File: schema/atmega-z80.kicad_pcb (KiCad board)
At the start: 2 copper layers, 62 parts, among them J1 USB Connector, J2 ISP Connector, Q1 PNP_2N4403, Q2 PNP_2N4403, Q3 NPN_2N4401, Q4 PNP_2N4403, U1 Z84C0010PEG, U2 ATmega324A-PU, U3 AS6C4008-55PCN, U4 SN74HC373N, U5 SN74HC257, U6 SN74HC257, U7 SN74HC00, U8 MCP2221AxP, Y1 20MHz

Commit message: update LED resistors
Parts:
- J2: value ISP Connector -> SPI Connector
- R16, R17: value 120 -> 220
- R18, R20: value 100 -> 200
- R22: value 100 -> 220
- R23: value 68 -> 200
- R25: value 22 -> 1K

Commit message: Preliminary PCB layout
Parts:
- removed the C10 at (122.7, 128.8)
- removed the R13 at (113.8, 92.7)
- added C8: 0.1uF, Capacitor_SMD:C_1206_3216Metric_Pad1.33x1.80mm_HandSolder, F.Cu at (113.5, 145.8)
- added D8: 1N5817, Diode_THT:D_DO-41_SOD81_P10.16mm_Horizontal, F.Cu at (142.7, 139.2)
- added D9: 1N5817, Diode_THT:D_DO-41_SOD81_P10.16mm_Horizontal, F.Cu at (142.7, 135.9)
- added J3: SPI Connector, Connector_PinHeader_2.54mm:PinHeader_1x06_P2.54mm_Vertical, F.Cu at (122.6, 45.1)
- added J4: I2C Connector, Connector_PinHeader_2.54mm:PinHeader_1x04_P2.54mm_Vertical, F.Cu at (122.7, 85.1)
- added R11: 10K, Resistor_SMD:R_1206_3216Metric_Pad1.30x1.75mm_HandSolder, F.Cu at (134.5, 53.0)
- added R14: 10K, Resistor_SMD:R_1206_3216Metric_Pad1.30x1.75mm_HandSolder, F.Cu at (137.1, 85.1)
- added R17: 39, Resistor_SMD:R_1206_3216Metric_Pad1.30x1.75mm_HandSolder, F.Cu at (110.1, 92.7)
- D1, D2, D3, D4, D5, D6, D7: footprint LED_THT:LED_D3.0mm -> LED_THT:LED_D5.0mm
- J2: value SPI Connector -> Programmer ISP 10
- R15: value 39 -> 10K
- moved R6 54.3 mm to (165.1, 45.0), turned to 180 degrees
- moved R7 54.2 mm to (165.1, 41.4), turned to 180 degrees
- moved R15 42.9 mm to (137.1, 92.7), turned to 0 degrees
- moved R12 34.9 mm to (134.5, 56.6)
- moved U4 32.8 mm to (179.7, 124.2), turned to 180 degrees
- moved U6 32.4 mm to (153.0, 124.3), turned to 180 degrees
- moved C5 31.4 mm to (208.7, 108.2), turned to 270 degrees
- moved U3 27.7 mm to (189.6, 44.5)
- moved SW_RESET1 25.9 mm to (99.1, 148.6)
- moved SW_USER1 25.9 mm to (80.5, 144.0)
- moved R5 24.3 mm to (165.1, 48.5)
- moved R4 24.3 mm to (165.1, 52.1)
- moved R3 24.3 mm to (165.1, 55.6)
- moved R2 24.2 mm to (165.1, 58.9)
- moved R1 24.2 mm to (165.1, 62.2)
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- renumbered C11 to C10, C12 to C11, C13 to C12, R11 to R13, R14 to R16, R16 to R18, R17 to R19, R18 to R20, R19 to R21, R20 to R22, R21 to R23, R22 to R24, R23 to R25, R24 to R26, R25 to R27, R26 to R28
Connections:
- net /SPI_MISO renamed SPI_MISO
- net /SPI_MOSI renamed SPI_MOSI
- net /SPI_SCK renamed SPI_SCK
- C9 pad 1: Net-(C9-Pad1) -> +5V
- R1 pad 2: /A6 -> /A4
- R10 pad 2: /A15 -> /A13
- R12 pad 1: +5V -> GND
- R12 pad 2: /#NMI -> /A15
- R15 pad 1: /#Z80_CLK -> +5V
- R15 pad 2: Net-(R15-Pad2) -> /#IORQ
- R2 pad 2: /A7 -> /A5
- R3 pad 2: /A8 -> /A6
- R4 pad 2: /A9 -> /A7
- R5 pad 2: /A10 -> /A8
- R6 pad 2: /A11 -> /A9
- R7 pad 2: /A12 -> /A10
- R8 pad 2: /A13 -> /A11
- R9 pad 2: /A14 -> /A12
- U2 pad 1: /A3 -> /A0
- U2 pad 14: /UART_RXD -> /ATMEGA_RX_AND_USB_TX
- U2 pad 15: /UART_TXD -> /ATMEGA_TX_AND_USB_RX
- U2 pad 2: /A4 -> /A1
- U2 pad 21: Net-(R15-Pad2) -> Net-(R17-Pad2)
- U2 pad 22: /D0 -> I2C_SCL
- U2 pad 23: /D1 -> I2C_SDA
- U2 pad 24: /D2 -> /#INT
- U2 pad 25: /D3 -> /#BUSRQ
- U2 pad 26: /D4 -> /#BUSACK
- U2 pad 27: /D5 -> /#WAIT
- U2 pad 28: /D6 -> /#R
- U2 pad 29: /D7 -> /CHANGE_BANK_ADDR
- U2 pad 3: /A5 -> /A2
- U2 pad 33: /A2 -> /D7
- U2 pad 34: /A1 -> /D6
- U2 pad 35: /A0 -> /D5
- U2 pad 36: /#R -> /D4
- U2 pad 37: /#WAIT -> /D3
- U2 pad 38: /#BUSACK -> /D2
- U2 pad 39: /#BUSRQ -> /D1
- U2 pad 4: /CHANGE_BANK_ADDR -> /A3
- U2 pad 40: /#INT -> /D0
- U2 pad 5: Net-(U2-Pad5) -> #SPI_SS
- U8 pad 11: Net-(C9-Pad1) -> Net-(C8-Pad1)
- U8 pad 3: USB_IO_LED -> Net-(D8-Pad2)
- U8 pad 5: /UART_RXD -> /ATMEGA_TX_AND_USB_RX
- U8 pad 6: /UART_TXD -> /ATMEGA_RX_AND_USB_TX
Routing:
- net +5V: track 0.00 -> 611.4 mm, vias 0 -> 1
- net #MEM_LED: track 0.00 -> 146.2 mm, vias 0 -> 6
- net /#SYS_RESET: track 0.00 -> 143.2 mm, vias 0 -> 1
- net /A3: track 0.00 -> 143.1 mm
- net /A2: track 0.00 -> 140.2 mm
- net /A1: track 0.00 -> 137.7 mm
- net /A0: track 0.00 -> 135.2 mm
- net /D7: track 0.00 -> 123.6 mm, vias 0 -> 1
- net #EXT_MEM_LED: track 0.00 -> 120.8 mm, vias 0 -> 2
- net /D0: track 0.00 -> 118.6 mm, vias 0 -> 3
- net /D6: track 0.00 -> 116.0 mm
- net /D1: track 0.00 -> 111.7 mm, vias 0 -> 3
- net /D4: track 0.00 -> 106.7 mm
- net /D5: track 0.00 -> 105.5 mm
- net /D2: track 0.00 -> 96.6 mm, vias 0 -> 2
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- added copper zone on B.Cu, net GND
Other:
- board outline added: 142.2 x 115.6 mm
- net class Power added: clearance 0.2, trace_width 0.5, via_dia 0.8, via_drill 0.4
- board text added: "+"

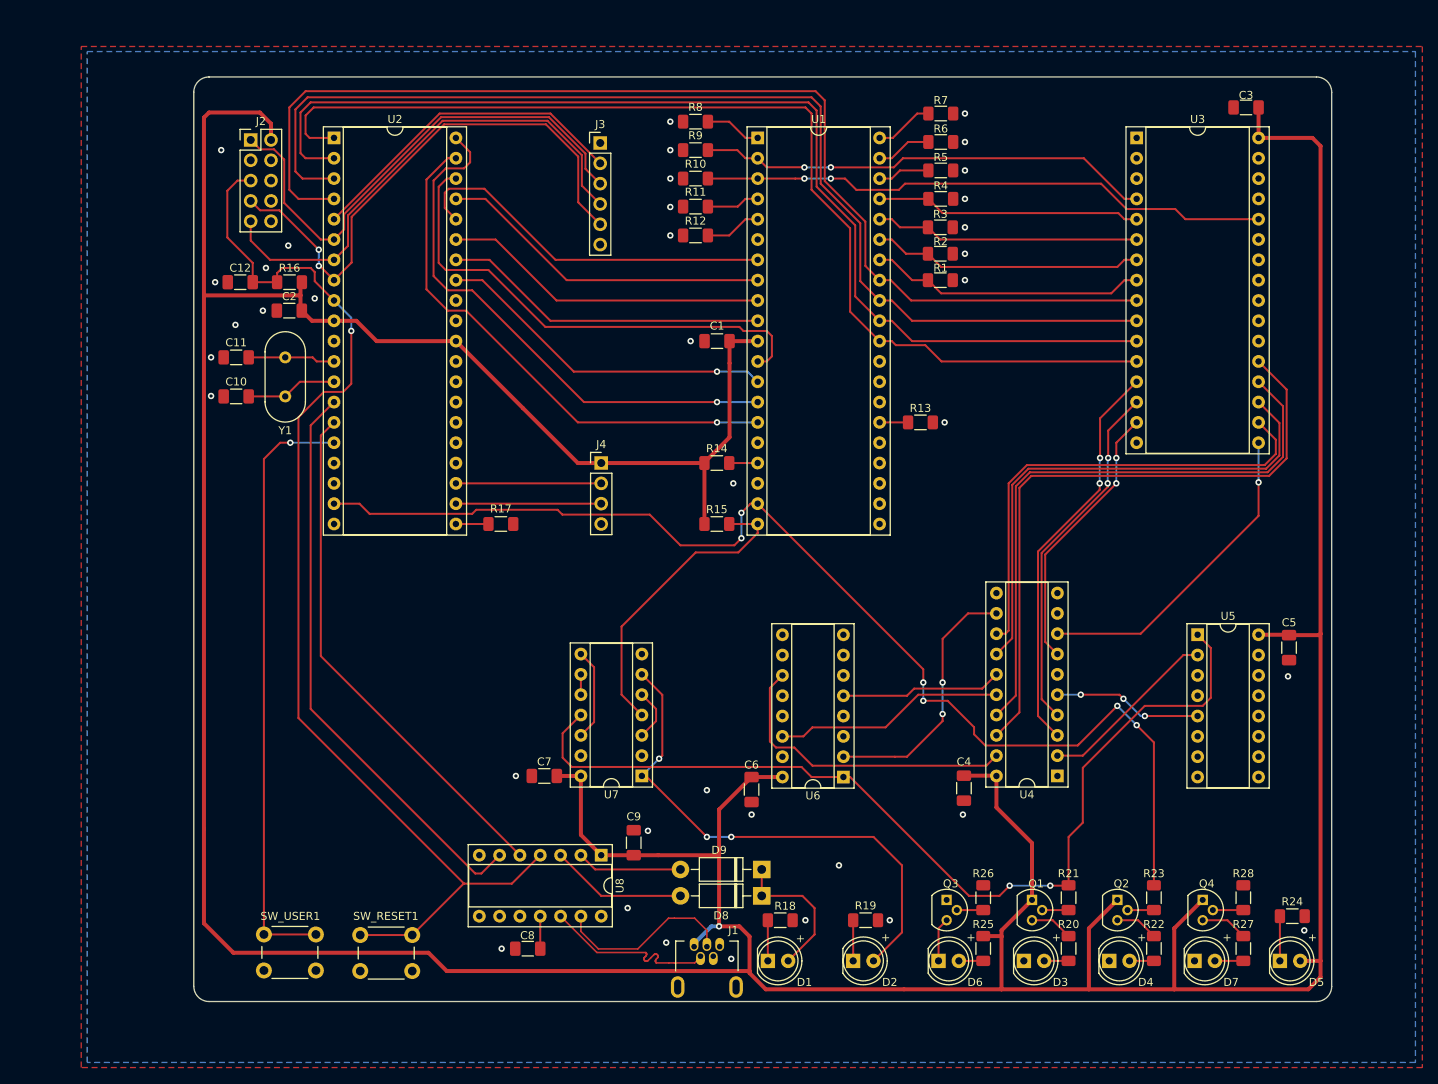
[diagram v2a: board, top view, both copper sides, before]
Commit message: Reversed all diodes on line USB_IO_LED because GP0 and GP1 of U8 are active low. (#4)
More PCB layout stuff.
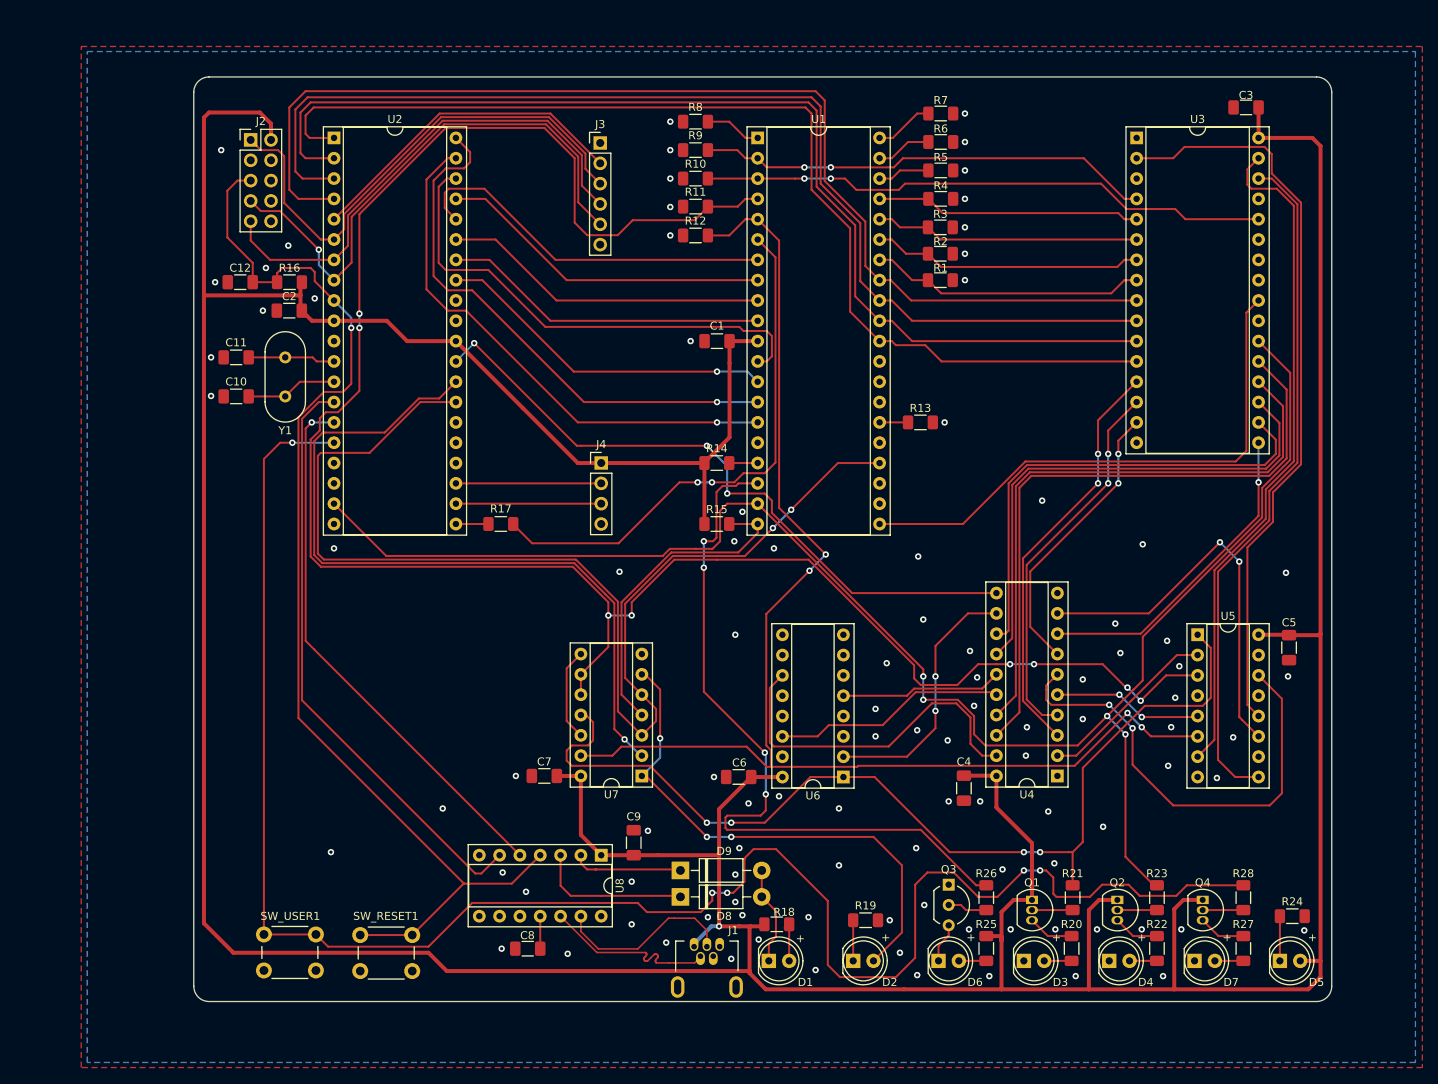
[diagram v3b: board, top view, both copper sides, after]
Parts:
- Q1, Q2, Q4: footprint Package_TO_SOT_THT:TO-92 -> Package_TO_SOT_THT:TO-92_Inline
- Q3: footprint Package_TO_SOT_THT:TO-92 -> Package_TO_SOT_THT:TO-92_Inline_Wide
- moved D9 10.2 mm to (132.6, 136.0), turned to 0 degrees
- moved D8 10.2 mm to (132.6, 139.3), turned to 0 degrees
- moved C6 2.25 mm to (139.9, 124.3), turned to 180 degrees
- moved Q3 1.92 mm to (166.1, 137.8)
- moved R18 0.67 mm to (144.6, 142.7), turned to 180 degrees
- moved R21 0.51 mm to (181.6, 139.4)
- moved R20 0.38 mm to (181.5, 145.8)
- moved R22 0.38 mm to (192.2, 145.8)
- moved R23 0.38 mm to (192.2, 139.4)
- moved R25 0.38 mm to (170.8, 145.8)
- moved R26 0.38 mm to (170.8, 139.4)
- moved D1 0.13 mm to (143.6, 147.3)
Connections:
- D1 pad 1: Net-(D1-Pad1) -> USB_IO_LED
- D1 pad 2: USB_IO_LED -> Net-(D1-Pad2)
- D8 pad 1: USB_IO_LED -> Net-(D8-Pad1)
- D8 pad 2: Net-(D8-Pad2) -> USB_IO_LED
- D9 pad 1: USB_IO_LED -> Net-(D9-Pad1)
- D9 pad 2: Net-(D9-Pad2) -> USB_IO_LED
- R18 pad 1: Net-(D1-Pad1) -> Net-(D1-Pad2)
- R18 pad 2: GND -> +5V
- U8 pad 2: Net-(D9-Pad2) -> Net-(D9-Pad1)
- U8 pad 3: Net-(D8-Pad2) -> Net-(D8-Pad1)
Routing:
- net /A14: track 9.16 -> 254.2 mm, vias 0 -> 8
- net /A15: track 7.06 -> 165.0 mm, vias 0 -> 4
- net #USER_LED: track 75.5 -> 229.2 mm, vias 1 -> 5
- net /#WAIT: track 6.55 -> 148.1 mm, vias 0 -> 2
- net /#R: track 0.00 -> 95.6 mm, vias 0 -> 1
- net Net-(U3-Pad2): track 0.00 -> 93.0 mm
- net Z80_ACTIVE_LED: track 0.00 -> 91.9 mm, vias 0 -> 4
- net Net-(U3-Pad30): track 0.00 -> 85.7 mm
- net Net-(U3-Pad31): track 0.00 -> 84.6 mm
- net /CHANGE_BANK_ADDR: track 0.00 -> 84.2 mm, vias 0 -> 3
- net /#RD: track 0.00 -> 69.1 mm
- net /#Z80_CLK: track 0.00 -> 66.8 mm, vias 0 -> 2
- net Net-(U4-Pad6): track 0.00 -> 57.9 mm, vias 0 -> 2
- net #MEM_LED: track 146.2 -> 203.2 mm, vias 6 -> 4
- net Net-(U4-Pad9): track 0.00 -> 50.3 mm, vias 0 -> 2
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
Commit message: A bunch of improvements / additions (#5)
* A bunch of improvements / additions
- PCB layout improvements
- 1N5817 diode datasheet
- CMake support
- ATMega program loader firmware
- program loader tool (z80_prog_loader.py)
- Z80 bootloader (bootloader.asm)
- Z80 sample program (blinky.asm)
- goose logo! (goose-icon.kicad_mod)
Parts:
- added G***: goose, atmega-z80:goose-icon, F.Cu at (90.7, 131.8)
- added H1: TopLeft, MountingHole:MountingHole_2.2mm_M2_DIN965_Pad, F.Cu at (74.4, 39.5)
- added H2: BottomLeft, MountingHole:MountingHole_2.2mm_M2_DIN965_Pad, F.Cu at (74.4, 149.7)
- added H3: TopRight, MountingHole:MountingHole_2.2mm_M2_DIN965_Pad, F.Cu at (211.3, 39.5)
- added H4: BottomRight, MountingHole:MountingHole_2.2mm_M2_DIN965_Pad, F.Cu at (208.8, 136.4)
- added R29: 1K, Resistor_SMD:R_1206_3216Metric_Pad1.30x1.75mm_HandSolder, F.Cu at (82.1, 138.2)
- added REF**: OSHW-Logo_11.4x12mm_SilkScreen, Symbol:OSHW-Logo_11.4x12mm_SilkScreen, F.Cu at (106.6, 109.6)
- C8: value 0.1uF -> 0.33uF
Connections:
- SW_USER1 pad 1: #USER_LED -> Net-(R29-Pad1)
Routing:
- net /A11: track 7.06 -> 81.2 mm, vias 0 -> 2
- net /D3: track 82.3 -> 155.6 mm, vias 1 -> 3
- net /D4: track 106.7 -> 178.4 mm, vias 0 -> 2
- net /A10: track 7.36 -> 69.9 mm
- net /A9: track 6.94 -> 63.9 mm, vias 0 -> 2
- net /A8: track 6.52 -> 51.4 mm, vias 0 -> 1
- net +5V: track 619.2 -> 662.4 mm, vias 1 -> 3
- net Net-(R29-Pad1): track 0.00 -> 12.3 mm
- net #USER_LED: track 229.2 -> 220.7 mm
- net /A0: track 135.2 -> 138.2 mm
- net /A3: track 143.1 -> 140.5 mm
- net /A12: track 57.1 -> 59.3 mm, vias 2 -> 3
- net /A2: track 140.2 -> 139.0 mm
- net /A1: track 137.7 -> 138.6 mm
- net /A13: track 71.6 -> 72.5 mm
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
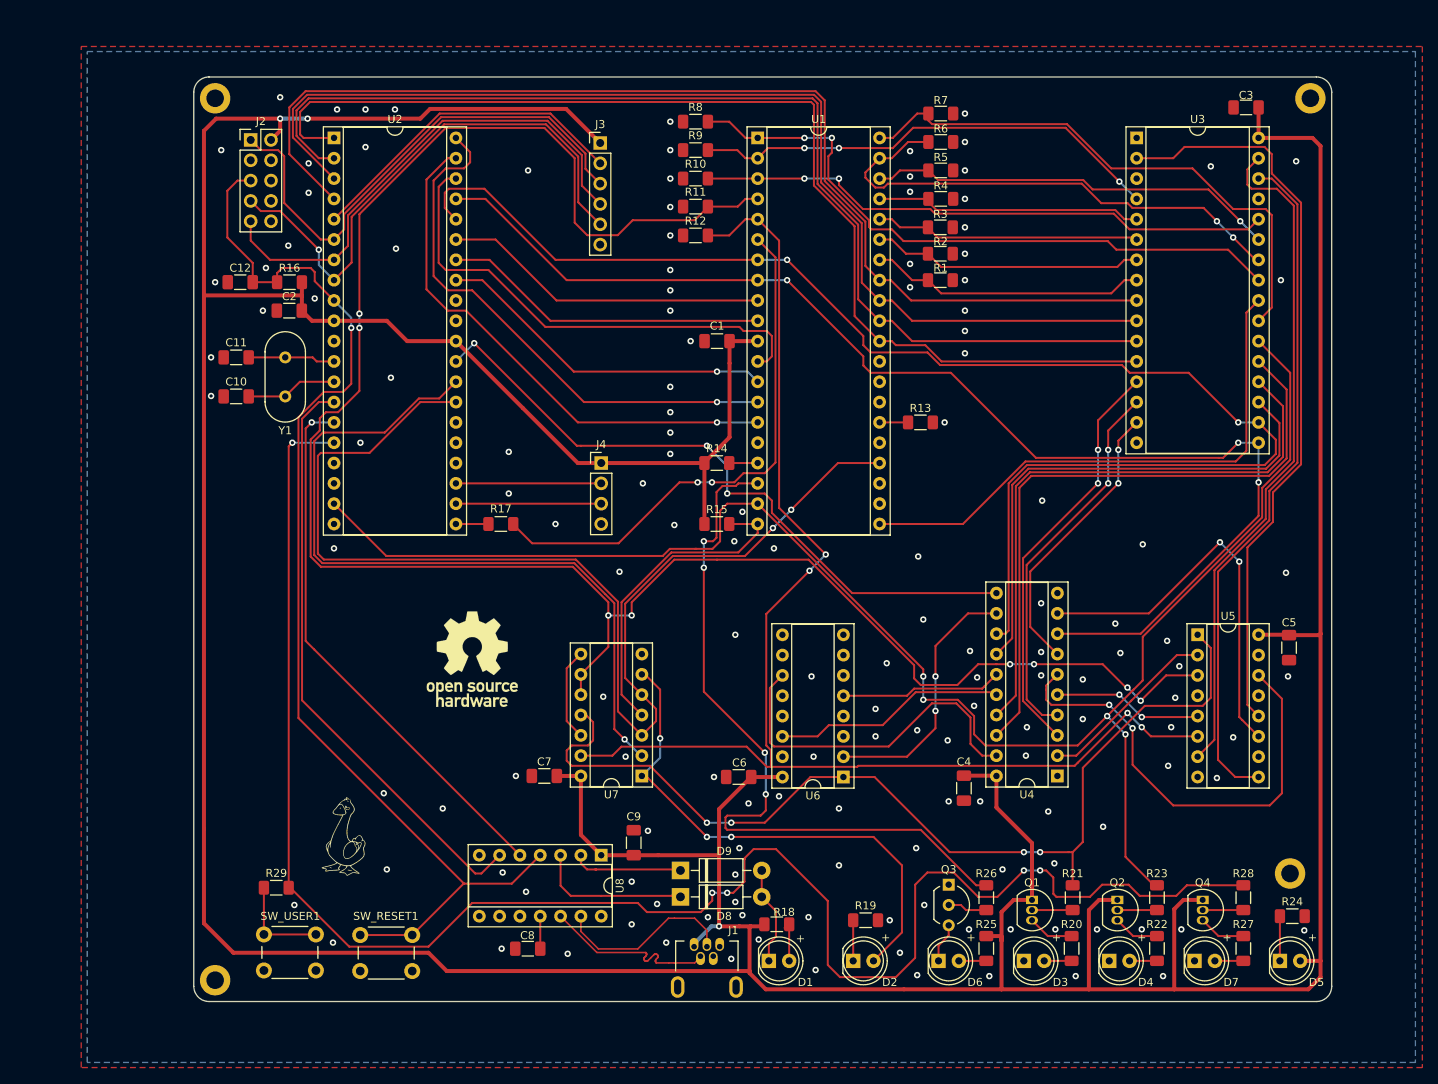
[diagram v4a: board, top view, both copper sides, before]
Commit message: PCB routing and Pasmo switch (#6)
* z80_prog_loader console output and memory banking support
memory banking logic bugfix
z80 hello world sample

* Changed #Z80_RESET line pull-down (R13) to pull-up

* Switched to Pasmo assembler

* Added console output handling to z80_prog_loader.py

* PCB routing complete
Minor improvements
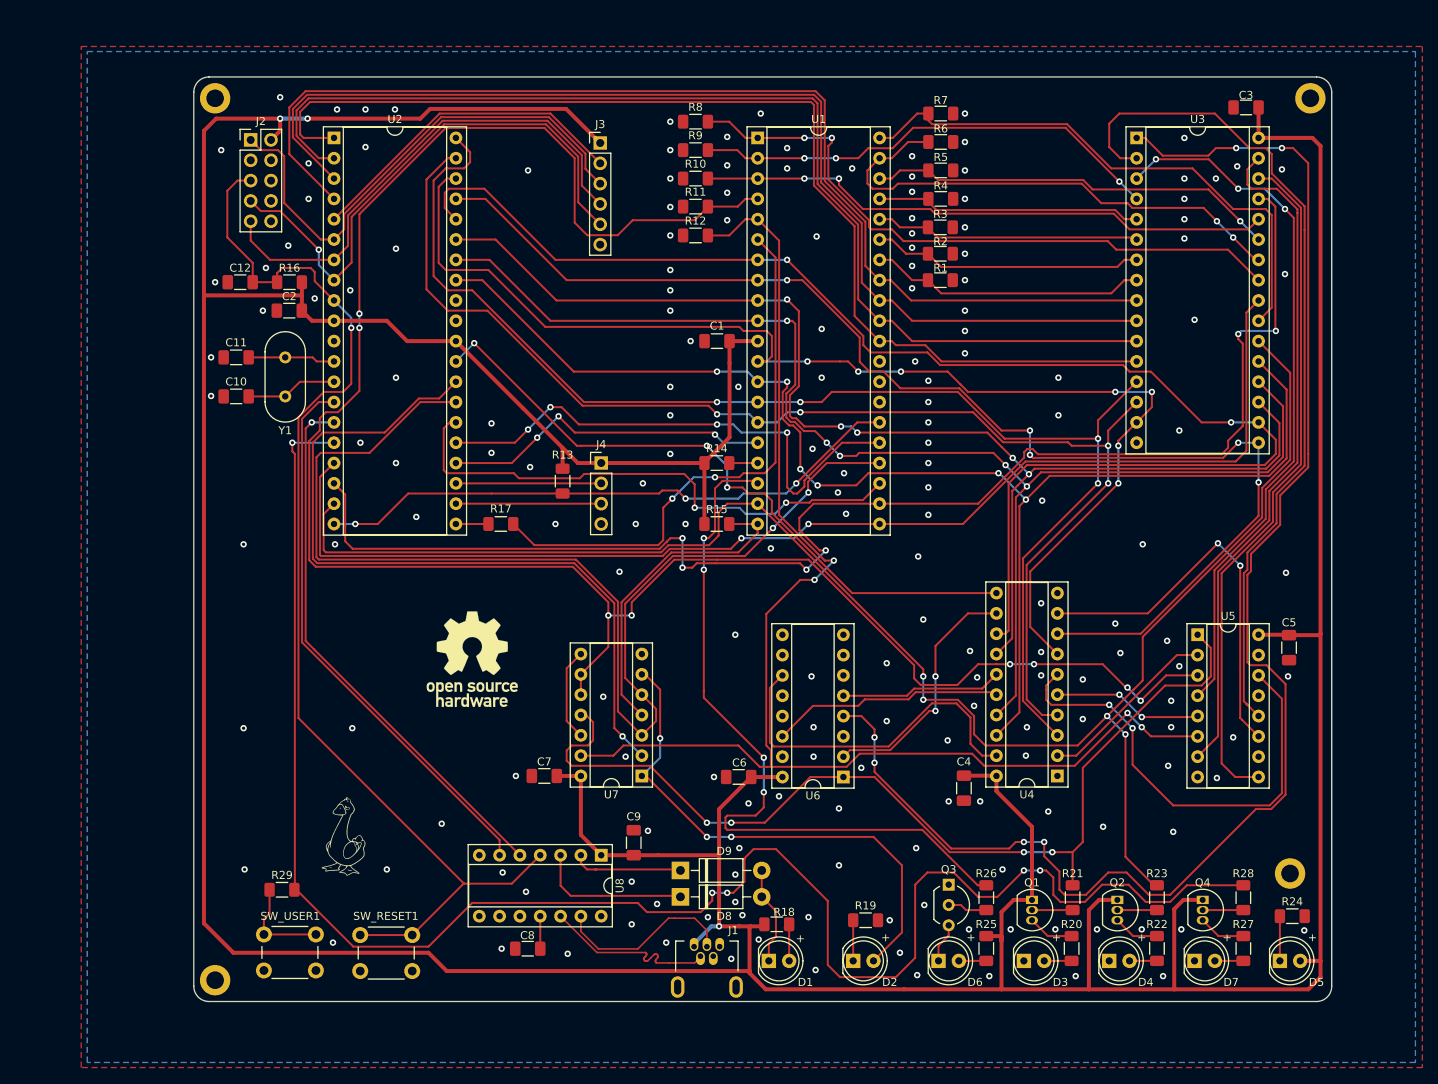
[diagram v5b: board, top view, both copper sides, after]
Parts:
- moved R13 45.3 mm to (117.9, 87.3), turned to 270 degrees
- moved R29 0.75 mm to (82.8, 138.4)
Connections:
- R13 pad 1: GND -> +5V
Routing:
- net Net-(U3-Pad1): track 0.00 -> 187.0 mm, vias 0 -> 6
- net /#WR: track 0.00 -> 176.3 mm, vias 0 -> 6
- net Net-(U3-Pad3): track 0.00 -> 88.4 mm, vias 0 -> 3
- net /#RD: track 69.1 -> 152.9 mm, vias 0 -> 2
- net /#Z80_RESET: track 3.56 -> 74.3 mm, vias 0 -> 3
- net /#BUSACK: track 0.00 -> 67.5 mm, vias 0 -> 2
- net /#BUSRQ: track 0.00 -> 66.4 mm, vias 0 -> 4
- net /D2: track 98.2 -> 153.6 mm, vias 2 -> 7
- net /D5: track 105.5 -> 157.3 mm, vias 0 -> 5
- net /D6: track 116.0 -> 166.2 mm, vias 0 -> 5
- net /D1: track 114.3 -> 160.4 mm, vias 3 -> 4
- net /D0: track 120.1 -> 165.6 mm, vias 3 -> 4
- net /D7: track 123.6 -> 169.1 mm, vias 1 -> 6
- net /#INT: track 0.00 -> 41.5 mm, vias 0 -> 3
- net Net-(U3-Pad2): track 93.0 -> 106.0 mm
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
